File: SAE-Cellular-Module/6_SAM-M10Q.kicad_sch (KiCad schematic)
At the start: 11 parts, among them U7 SAM-M10Q-00B

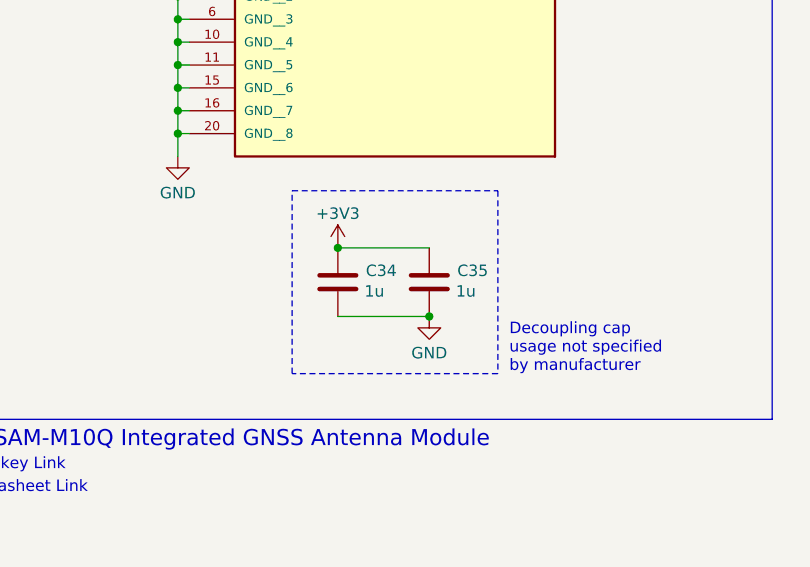
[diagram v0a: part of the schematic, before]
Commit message: Added initial component placements
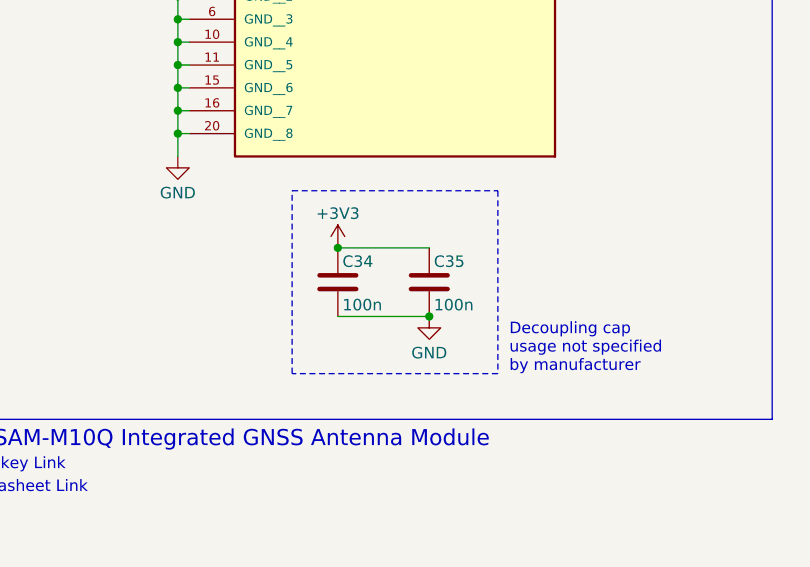
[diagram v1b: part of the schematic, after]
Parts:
- C34, C35: value 1u -> 100n; footprint (none) -> Capacitor_SMD:C_0402_1005Metric; MPN (none) -> CL05B104KP5NNNC
- TP35, TP36, TP37, TP38, TP39, TP40, TP41, TP42: footprint (none) -> TestPoint:TestPoint_Pad_D1.0mm
- U7: MPN (none) -> SAM-M10Q-00B
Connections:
- net +3V3: now also C34.1, C35.1; no longer C34.2, C35.2
- net GND: now also C34.2, C35.2; no longer C34.1, C35.1
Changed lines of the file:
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@@
+	)
+	(junction
+		(at 124.46 83.82)
+		(diameter 0)
+		(color 0 0 0 0)
+	)
+	(junction
+		(at 132.08 106.68)
+		(diameter 0)
+		(color 0 0 0 0)
+	)
+	(junction
+		(at 132.08 99.06)
+		(diameter 0)
+		(color 0 0 0 0)
 	)
 	(junction
@@
 	)
 	(junction
-		(at 124.46 83.82)
-		(diameter 0)
-		(color 0 0 0 0)
-	)
-	(junction
-		(at 132.08 106.68)
-		(diameter 0)
-		(color 0 0 0 0)
-	)
-	(junction
-		(at 132.08 99.06)
-		(diameter 0)
-		(color 0 0 0 0)
-	)
-	(junction
 		(at 132.08 96.52)
 		(diameter 0)
@@
 	)
 	(junction
-		(at 149.86 121.92)
-		(diameter 0)
-		(color 0 0 0 0)
-	)
-	(junction
 		(at 180.34 68.58)
 		(diameter 0)
@@
 	(junction
 		(at 128.27 81.28)
+		(diameter 0)
+		(color 0 0 0 0)
+	)
+	(junction
+		(at 149.86 121.92)
 		(diameter 0)
 		(color 0 0 0 0)
@@
 			)
 		)
-		(property "Footprint" ""
+		(property "Footprint" "TestPoint:TestPoint_Pad_D1.0mm"
 			(at 133.35 81.28 0)
 			(effects
@@
 			)
 		)
-		(property "Footprint" ""
+		(property "Footprint" "TestPoint:TestPoint_Pad_D1.0mm"
 			(at 133.35 78.74 0)
 			(effects
@@
 			)
 		)
-		(property "Footprint" ""
+		(property "Footprint" "TestPoint:TestPoint_Pad_D1.0mm"
 			(at 175.26 68.58 0)
 			(effects
@@
 			)
 		)
+		(property "MPN" "SAM-M10Q-00B"
+			(at 156.21 73.66 0)
+			(effects
+				(font
+					(size 1.27 1.27)
+				)
+				(hide yes)
+			)
+		)
 		(pin "6"
 		)
@@
 			)
 		)
-		(property "Footprint" ""
+		(property "Footprint" "TestPoint:TestPoint_Pad_D1.0mm"
 			(at 185.42 78.74 0)
 			(effects
@@
 	)
 	(symbol
-		(lib_id "Device:C")
-		(at 149.86 125.73 180)
-		(unit 1)
-		(exclude_from_sim no)
-		(in_bom yes)
-		(on_board yes)
-		(dnp no)
-		(property "Reference" "C34"
-			(at 154.686 124.46 0)
-			(effects
-				(font
-					(size 1.27 1.27)
-				)
-			)
-		)
-		(property "Value" "1u"
-			(at 153.924 126.746 0)
-			(effects
-				(font
-					(size 1.27 1.27)
-				)
-			)
-		)
-		(property "Footprint" ""
-			(at 148.8948 121.92 0)
-			(effects
-				(font
-					(size 1.27 1.27)
-				)
-				(hide yes)
-			)
-		)
-		(property "Datasheet" "~"
-			(at 149.86 125.73 0)
-			(effects
-				(font
-					(size 1.27 1.27)
-				)
-				(hide yes)
-			)
-		)
-		(property "Description" "Unpolarized capacitor"
-			(at 149.86 125.73 0)
-			(effects
-				(font
-					(size 1.27 1.27)
-				)
-				(hide yes)
-			)
-		)
-		(pin "1"
-		)
-		(pin "2"
-		)
-		(instances
-			(project ""
-				(path "/a08fab55-11db-44fb-b9aa-270892bf89c0/3fbbcbd0-9713-48e9-bad3-cec99a2b6181"
-					(reference "C34")
-					(unit 1)
-				)
-			)
-		)
-	)
-	(symbol
 		(lib_id "Connector:TestPoint")
 		(at 179.07 73.66 270)
@@
 			)
 		)
-		(property "Footprint" ""
+		(property "Footprint" "TestPoint:TestPoint_Pad_D1.0mm"
 			(at 179.07 68.58 0)
 			(effects
@@
 			)
 		)
-		(property "Footprint" ""
+		(property "Footprint" "TestPoint:TestPoint_Pad_D1.0mm"
 			(at 129.54 87.63 0)
 			(effects
@@
 			)
 		)
-		(property "Footprint" ""
+		(property "Footprint" "TestPoint:TestPoint_Pad_D1.0mm"
 			(at 133.35 85.09 0)
 			(effects
@@
 				(path "/a08fab55-11db-44fb-b9aa-270892bf89c0/3fbbcbd0-9713-48e9-bad3-cec99a2b6181"
 					(reference "TP41")
+					(unit 1)
+				)
+			)
+		)
+	)
+	(symbol
+		(lib_id "Device:C")
+		(at 149.86 125.73 0)
+		(unit 1)
+		(exclude_from_sim no)
+		(in_bom yes)
+		(on_board yes)
+		(dnp no)
+		(property "Reference" "C34"
+			(at 150.368 123.444 0)
+			(effects
+				(font
+					(size 1.27 1.27)
+				)
+				(justify left)
+			)
+		)
+		(property "Value" "100n"
+			(at 150.368 128.27 0)
+			(effects
+				(font
+					(size 1.27 1.27)
+				)
+				(justify left)
+			)
+		)
+		(property "Footprint" "Capacitor_SMD:C_0402_1005Metric"
+			(at 150.8252 129.54 0)
+			(effects
+				(font
+					(size 1.27 1.27)
+				)
+				(hide yes)
+			)
+		)
+		(property "Datasheet" "~"
+			(at 149.86 125.73 0)
+			(effects
+				(font
+					(size 1.27 1.27)
+				)
+				(hide yes)
+			)
+		)
+		(property "Description" "Unpolarized capacitor"
+			(at 149.86 125.73 0)
+			(effects
+				(font
+					(size 1.27 1.27)
+				)
+				(hide yes)
+			)
+		)
+		(property "MPN" "CL05B104KP5NNNC"
+			(at 149.86 125.73 0)
+			(effects
+				(font
+					(size 1.27 1.27)
+				)
+				(hide yes)
+			)
+		)
+		(pin "2"
+		)
+		(pin "1"
+		)
+		(instances
+			(project "SAE Cellular Module"
+				(path "/a08fab55-11db-44fb-b9aa-270892bf89c0/3fbbcbd0-9713-48e9-bad3-cec99a2b6181"
+					(reference "C34")
 					(unit 1)
 				)
@@
 			)
 		)
-		(property "Footprint" ""
+		(property "Footprint" "TestPoint:TestPoint_Pad_D1.0mm"
 			(at 133.35 73.66 0)
 			(effects
@@
 				(path "/a08fab55-11db-44fb-b9aa-270892bf89c0/3fbbcbd0-9713-48e9-bad3-cec99a2b6181"
 					(reference "TP35")
+					(unit 1)
+				)
+			)
+		)
+	)
+	(symbol
+		(lib_id "Device:C")
+		(at 160.02 125.73 0)
+		(unit 1)
+		(exclude_from_sim no)
+		(in_bom yes)
+		(on_board yes)
+		(dnp no)
+		(property "Reference" "C35"
+			(at 160.528 123.444 0)
+			(effects
+				(font
+					(size 1.27 1.27)
+				)
+				(justify left)
+			)
+		)
+		(property "Value" "100n"
+			(at 160.528 128.27 0)
+			(effects
+				(font
+					(size 1.27 1.27)
+				)
+				(justify left)
+			)
+		)
+		(property "Footprint" "Capacitor_SMD:C_0402_1005Metric"
+			(at 160.9852 129.54 0)
+			(effects
+				(font
+					(size 1.27 1.27)
+				)
+				(hide yes)
+			)
+		)
+		(property "Datasheet" "~"
+			(at 160.02 125.73 0)
+			(effects
+				(font
+					(size 1.27 1.27)
+				)
+				(hide yes)
+			)
+		)
+		(property "Description" "Unpolarized capacitor"
+			(at 160.02 125.73 0)
+			(effects
+				(font
+					(size 1.27 1.27)
+				)
+				(hide yes)
+			)
+		)
+		(property "MPN" "CL05B104KP5NNNC"
+			(at 160.02 125.73 0)
+			(effects
+				(font
+					(size 1.27 1.27)
+				)
+				(hide yes)
+			)
+		)
+		(pin "2"
+		)
+		(pin "1"
+		)
+		(instances
+			(project "SAE Cellular Module"
+				(path "/a08fab55-11db-44fb-b9aa-270892bf89c0/3fbbcbd0-9713-48e9-bad3-cec99a2b6181"
+					(reference "C35")
 					(unit 1)
 				)
@@
 					(unit 1)
 				)
-			)
-		)
-	)
-	(symbol
-		(lib_id "Device:C")
-		(at 160.02 125.73 180)
-		(unit 1)
-		(exclude_from_sim no)
-		(in_bom yes)
-		(on_board yes)
-		(dnp no)
-		(property "Reference" "C35"
-			(at 164.846 124.46 0)
-			(effects
-				(font
-					(size 1.27 1.27)
-				)
-			)
-		)
-		(property "Value" "1u"
-			(at 164.084 126.746 0)
-			(effects
-				(font
-					(size 1.27 1.27)
-				)
-			)
-		)
-		(property "Footprint" ""
-			(at 159.0548 121.92 0)
-			(effects
-				(font
-					(size 1.27 1.27)
-				)
-				(hide yes)
-			)
-		)
-		(property "Datasheet" "~"
-			(at 160.02 125.73 0)
-			(effects
-				(font
-					(size 1.27 1.27)
-				)
-				(hide yes)
-			)
-		)
-		(property "Description" "Unpolarized capacitor"
-			(at 160.02 125.73 0)
-			(effects
-				(font
-					(size 1.27 1.27)
-				)
-				(hide yes)
-			)
-		)
-		(pin "1"
-		)
-		(pin "2"
-		)
-		(instances
-			(project "SAE Cellular Module"
-				(path "/a08fab55-11db-44fb-b9aa-270892bf89c0/3fbbcbd0-9713-48e9-bad3-cec99a2b6181"
-					(reference "C35")
-					(unit 1)
-				)
